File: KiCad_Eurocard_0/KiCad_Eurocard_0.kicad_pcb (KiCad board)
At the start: 2 copper layers, 1 part, among them IC1 ERA-1SM+

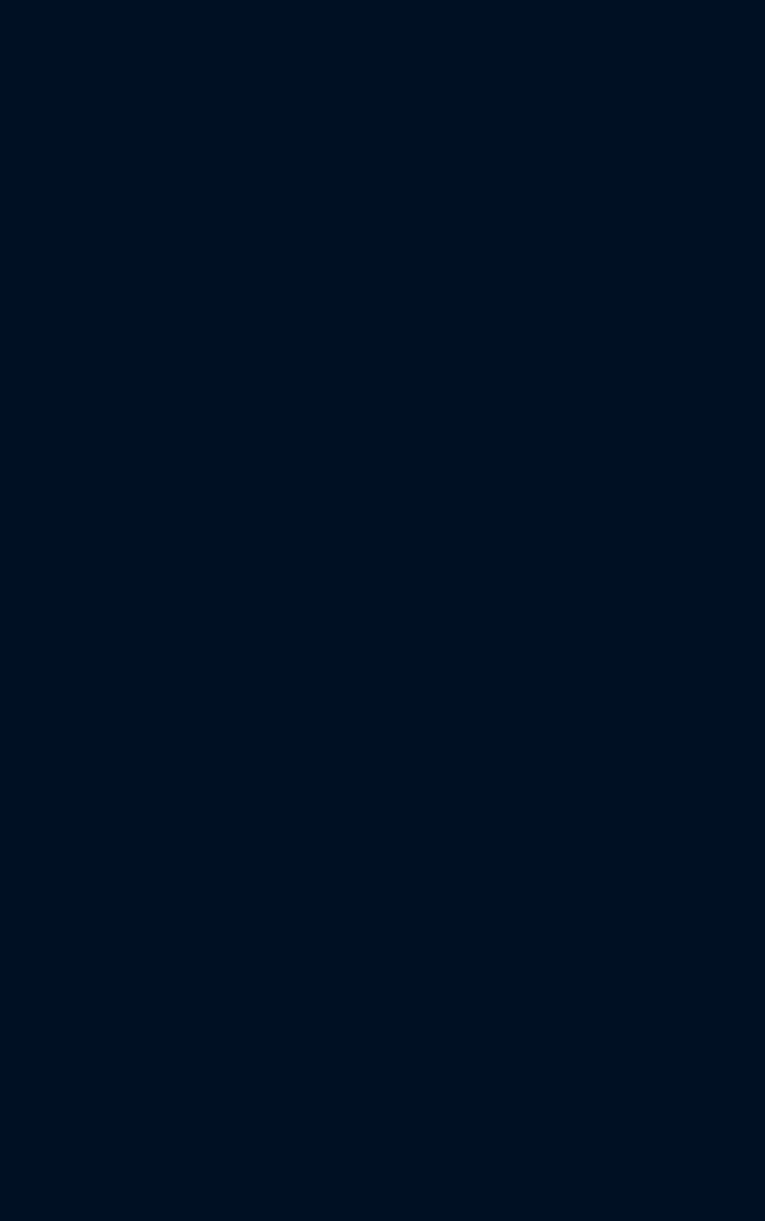
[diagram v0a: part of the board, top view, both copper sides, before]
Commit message: New Additions - Added new footprints
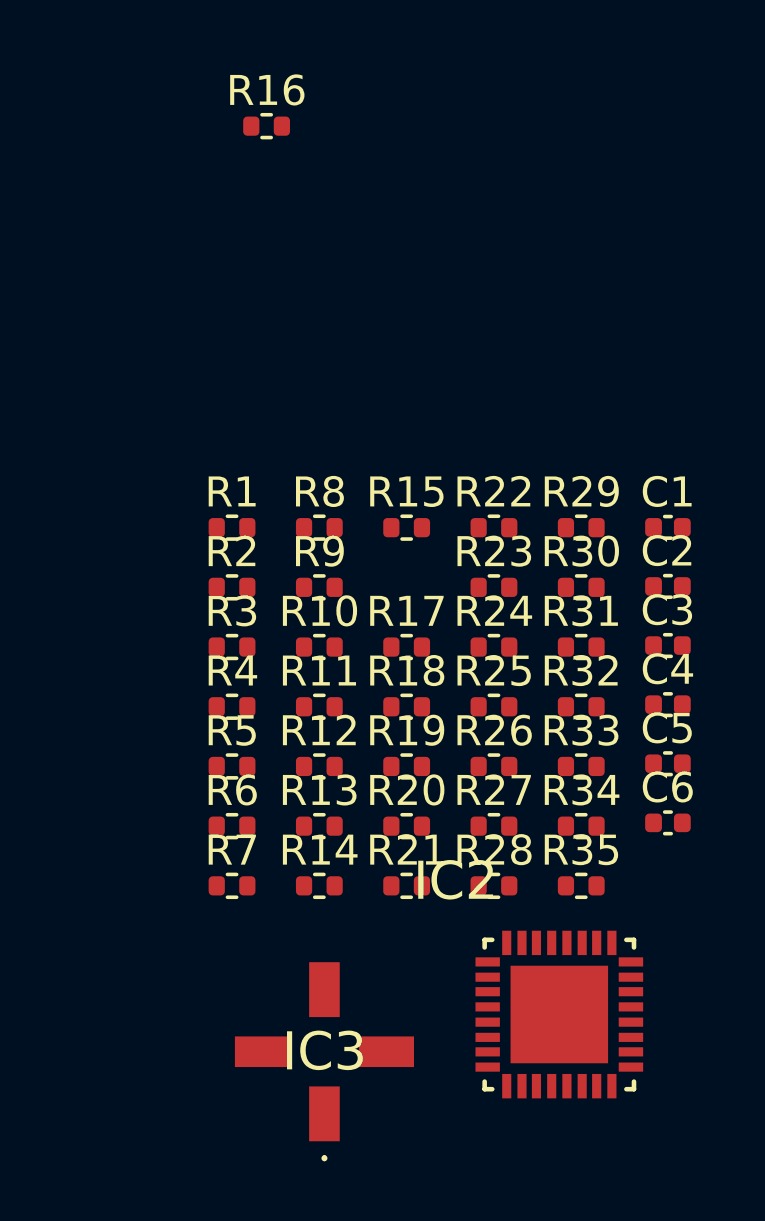
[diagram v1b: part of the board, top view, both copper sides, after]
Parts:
- added C1: C, Capacitor_SMD:C_0402_1005Metric, F.Cu at (108.9, 58.4)
- added C2: C, Capacitor_SMD:C_0402_1005Metric, F.Cu at (108.9, 60.3)
- added C3: C, Capacitor_SMD:C_0402_1005Metric, F.Cu at (108.9, 62.3)
- added C4: C, Capacitor_SMD:C_0402_1005Metric, F.Cu at (108.9, 64.3)
- added C5: C, Capacitor_SMD:C_0402_1005Metric, F.Cu at (108.9, 66.3)
- added C6: C, Capacitor_SMD:C_0402_1005Metric, F.Cu at (108.9, 68.2)
- added IC2: ADF4351BCPZ, ADF4351BPCZ:QFN50P500X500X100-33N, F.Cu at (105.2, 74.6)
- added IC3: ERA-1SM+, ERA-1SM+:ERA1SM, F.Cu at (97.4, 75.9)
- added R1: R, Resistor_SMD:R_0402_1005Metric, F.Cu at (94.3, 58.4)
- added R10: R, Resistor_SMD:R_0402_1005Metric, F.Cu at (97.2, 62.4)
- added R11: R, Resistor_SMD:R_0402_1005Metric, F.Cu at (97.2, 64.4)
- added R12: R, Resistor_SMD:R_0402_1005Metric, F.Cu at (97.2, 66.3)
- added R13: R, Resistor_SMD:R_0402_1005Metric, F.Cu at (97.2, 68.3)
- added R14: R, Resistor_SMD:R_0402_1005Metric, F.Cu at (97.2, 70.3)
- added R15: R, Resistor_SMD:R_0402_1005Metric, F.Cu at (100.2, 58.4)
- added R16: R, Resistor_SMD:R_0402_1005Metric, F.Cu at (95.5, 45.0)
- added R17: R, Resistor_SMD:R_0402_1005Metric, F.Cu at (100.2, 62.4)
- added R18: R, Resistor_SMD:R_0402_1005Metric, F.Cu at (100.2, 64.4)
- added R19: R, Resistor_SMD:R_0402_1005Metric, F.Cu at (100.2, 66.3)
- added R2: R, Resistor_SMD:R_0402_1005Metric, F.Cu at (94.3, 60.4)
- added R20: R, Resistor_SMD:R_0402_1005Metric, F.Cu at (100.2, 68.3)
- added R21: R, Resistor_SMD:R_0402_1005Metric, F.Cu at (100.2, 70.3)
- added R22: R, Resistor_SMD:R_0402_1005Metric, F.Cu at (103.1, 58.4)
- added R23: R, Resistor_SMD:R_0402_1005Metric, F.Cu at (103.1, 60.4)
- added R24: R, Resistor_SMD:R_0402_1005Metric, F.Cu at (103.1, 62.4)
- added R25: R, Resistor_SMD:R_0402_1005Metric, F.Cu at (103.1, 64.4)
- added R26: R, Resistor_SMD:R_0402_1005Metric, F.Cu at (103.1, 66.3)
- added R27: R, Resistor_SMD:R_0402_1005Metric, F.Cu at (103.1, 68.3)
- added R28: R, Resistor_SMD:R_0402_1005Metric, F.Cu at (103.1, 70.3)
- added R29: R, Resistor_SMD:R_0402_1005Metric, F.Cu at (106.0, 58.4)
- added R3: R, Resistor_SMD:R_0402_1005Metric, F.Cu at (94.3, 62.4)
- added R30: R, Resistor_SMD:R_0402_1005Metric, F.Cu at (106.0, 60.4)
- added R31: R, Resistor_SMD:R_0402_1005Metric, F.Cu at (106.0, 62.4)
- added R32: R, Resistor_SMD:R_0402_1005Metric, F.Cu at (106.0, 64.4)
- added R33: R, Resistor_SMD:R_0402_1005Metric, F.Cu at (106.0, 66.3)
- added R34: R, Resistor_SMD:R_0402_1005Metric, F.Cu at (106.0, 68.3)
- added R35: R, Resistor_SMD:R_0402_1005Metric, F.Cu at (106.0, 70.3)
- added R4: R, Resistor_SMD:R_0402_1005Metric, F.Cu at (94.3, 64.4)
- added R5: R, Resistor_SMD:R_0402_1005Metric, F.Cu at (94.3, 66.3)
- added R6: R, Resistor_SMD:R_0402_1005Metric, F.Cu at (94.3, 68.3)
- added R7: R, Resistor_SMD:R_0402_1005Metric, F.Cu at (94.3, 70.3)
- added R8: R, Resistor_SMD:R_0402_1005Metric, F.Cu at (97.2, 58.4)
- added R9: R, Resistor_SMD:R_0402_1005Metric, F.Cu at (97.2, 60.4)
- IC1: footprint KiCad:ERA1SM -> ERA-1SM+:ERA1SM
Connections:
- IC1 pad 1: unconnected-(IC1-RF_IN-Pad1) -> Net-(IC1-RF_IN)
- IC1 pad 2: unconnected-(IC1-GND_1-Pad2) -> GND
- IC1 pad 3: unconnected-(IC1-RF_-_OUT_AND_DC_-_IN-Pad3) -> Net-(IC1-RF_-_OUT_AND_DC_-_IN)
- IC1 pad 4: unconnected-(IC1-GND_2-Pad4) -> GND

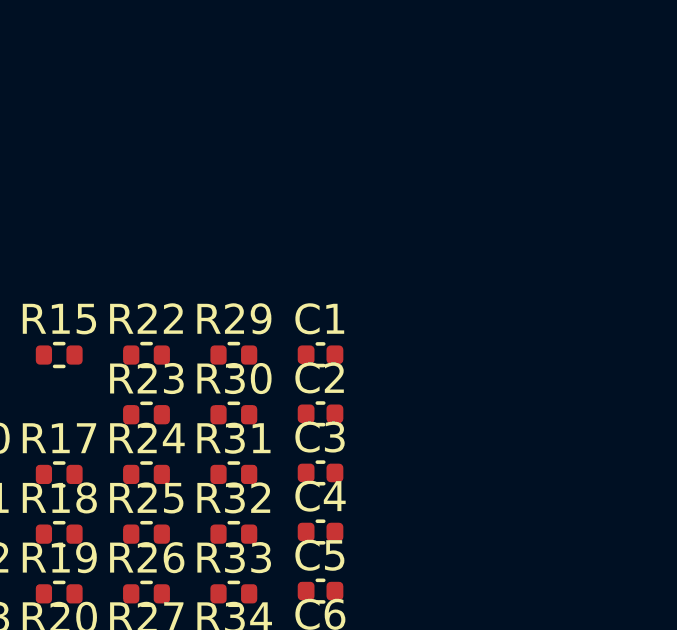
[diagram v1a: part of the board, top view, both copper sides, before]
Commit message: Changed wires to gobal nets
still need to figure out DDS and ADF4351
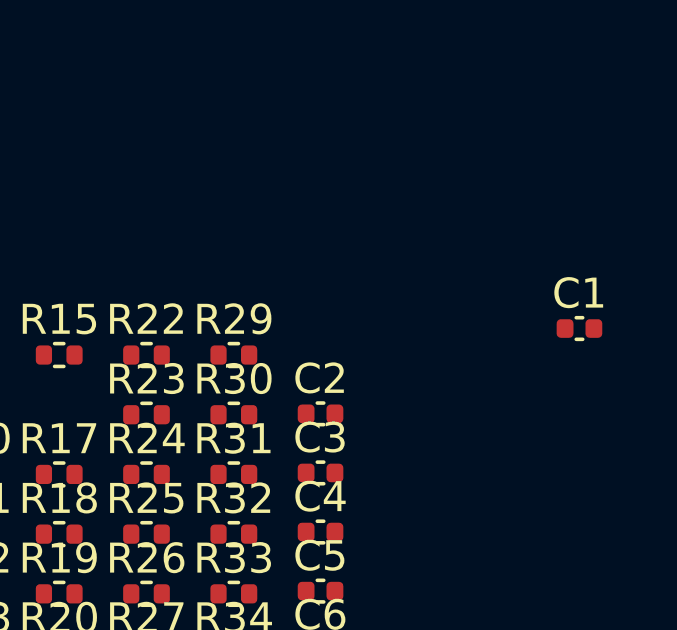
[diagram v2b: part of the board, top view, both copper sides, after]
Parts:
- moved C1 8.68 mm to (117.5, 57.5)
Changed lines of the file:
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@@
 	(footprint "Capacitor_SMD:C_0402_1005Metric"
 		(layer "F.Cu")
-		(at 108.8684 58.3734)
+		(at 117.5 57.5)
 		(descr "Capacitor SMD 0402 (1005 Metric), square (rectangular) end terminal, IPC-7351 nominal, (Body size source: IPC-SM-782 page 76, https://www.pcb-3d.com/wordpress/wp-content/uploads/ipc-sm-782a_amendment_1_and_2.pdf), generated with kicad-footprint-generator")
 		(tags "capacitor")

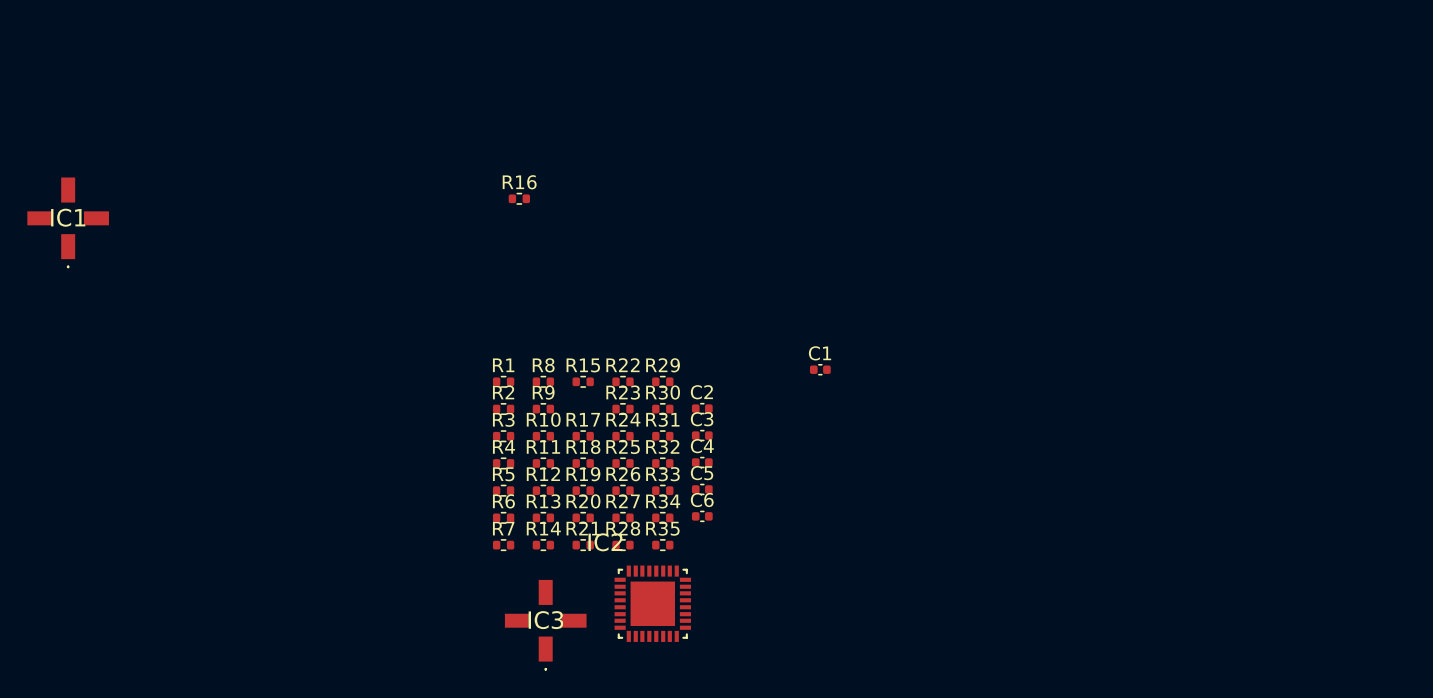
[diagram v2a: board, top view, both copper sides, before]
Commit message: ADF4351 Microcontroller Connecs. Done
- Added Microcontroller and connections to the ADF4351
- Started parameters note sheet
- Need to double check power is sufficient for circuit (hopefully, we can just use the 5V USB to power everything?)
- Need to make schematic look pretty as well/be more organized/labeled
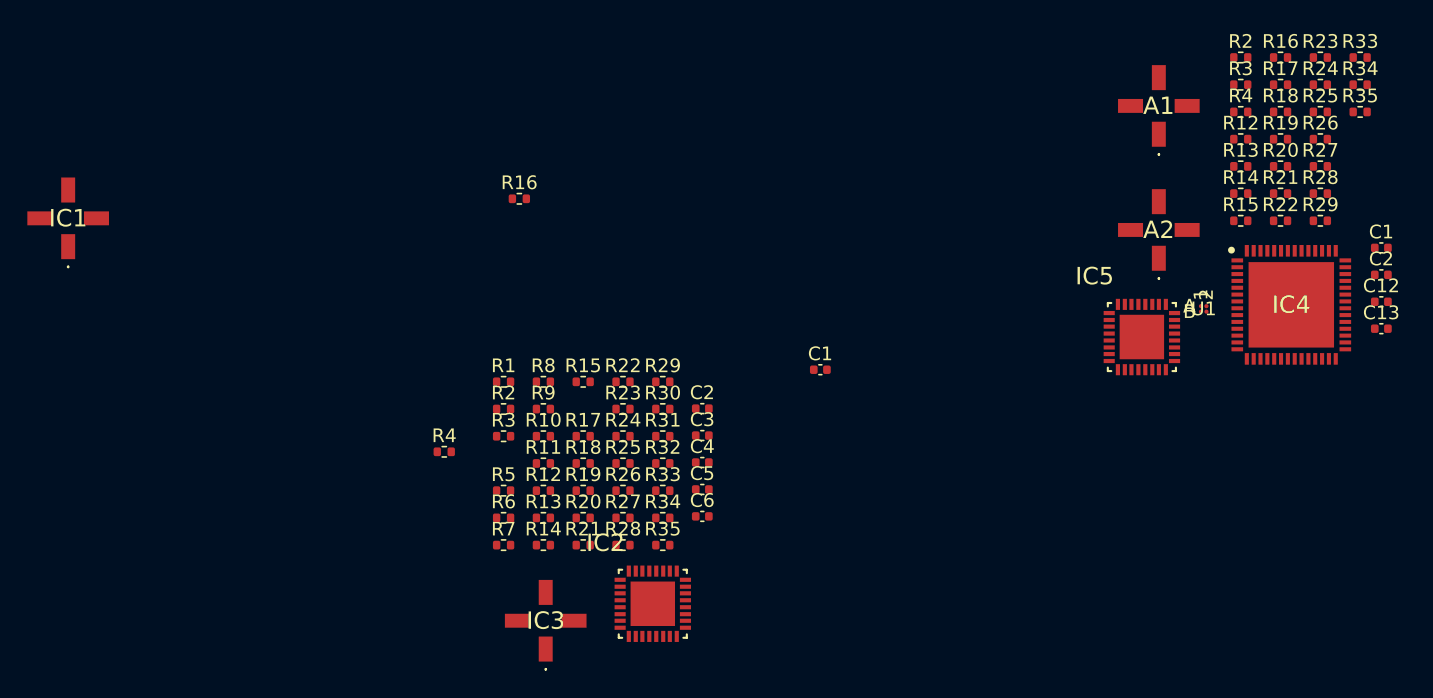
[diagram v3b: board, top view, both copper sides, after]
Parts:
- added A1: ERA-1SM+, ERA-1SM+:ERA1SM, F.Cu at (142.2, 38.2)
- added A2: ERA-1SM+, ERA-1SM+:ERA1SM, F.Cu at (142.2, 47.3)
- added C1: 300pF, Capacitor_SMD:C_0402_1005Metric, F.Cu at (158.5, 48.6)
- added C12: 300pF, Capacitor_SMD:C_0402_1005Metric, F.Cu at (158.5, 52.5)
- added C13: 300pF, Capacitor_SMD:C_0402_1005Metric, F.Cu at (158.5, 54.5)
- added C2: 300pF, Capacitor_SMD:C_0402_1005Metric, F.Cu at (158.5, 50.6)
- added IC4: AD9959BCPZ, KiCad:QFN50P800X800X100-57N-D, F.Cu at (151.9, 52.8)
- added IC5: ADF4351BCPZ, ADF4351BPCZ:QFN50P500X500X100-33N, F.Cu at (141.0, 55.1)
- added R12: 292.4 Ohms, Resistor_SMD:R_0402_1005Metric, F.Cu at (148.2, 40.6)
- added R13: 292.4 Ohms, Resistor_SMD:R_0402_1005Metric, F.Cu at (148.2, 42.6)
- added R14: 17.6 Ohms, Resistor_SMD:R_0402_1005Metric, F.Cu at (148.2, 44.6)
- added R15: 292.4 Ohms, Resistor_SMD:R_0402_1005Metric, F.Cu at (148.2, 46.6)
- added R16: 292.4 Ohms, Resistor_SMD:R_0402_1005Metric, F.Cu at (151.2, 34.7)
- added R17: 17.6 Ohms, Resistor_SMD:R_0402_1005Metric, F.Cu at (151.2, 36.7)
- added R18: 292.4 Ohms, Resistor_SMD:R_0402_1005Metric, F.Cu at (151.2, 38.6)
- added R19: 292.4 Ohms, Resistor_SMD:R_0402_1005Metric, F.Cu at (151.2, 40.6)
- added R2: 116.1 Ohms, Resistor_SMD:R_0402_1005Metric, F.Cu at (148.2, 34.7)
- added R20: 17.6 Ohms, Resistor_SMD:R_0402_1005Metric, F.Cu at (151.2, 42.6)
- added R21: 292.4 Ohms, Resistor_SMD:R_0402_1005Metric, F.Cu at (151.2, 44.6)
- added R22: 292.4 Ohms, Resistor_SMD:R_0402_1005Metric, F.Cu at (151.2, 46.6)
- added R23: 17.6 Ohms, Resistor_SMD:R_0402_1005Metric, F.Cu at (154.1, 34.7)
- added R24: 292.4 Ohms, Resistor_SMD:R_0402_1005Metric, F.Cu at (154.1, 36.7)
- added R25: 292.4 Ohms, Resistor_SMD:R_0402_1005Metric, F.Cu at (154.1, 38.6)
- added R26: 17.6 Ohms, Resistor_SMD:R_0402_1005Metric, F.Cu at (154.1, 40.6)
- added R27: 292.4 Ohms, Resistor_SMD:R_0402_1005Metric, F.Cu at (154.1, 42.6)
- added R28: 292.4 Ohms, Resistor_SMD:R_0402_1005Metric, F.Cu at (154.1, 44.6)
- added R29: 17.6 Ohms, Resistor_SMD:R_0402_1005Metric, F.Cu at (154.1, 46.6)
- added R3: 52.8 Ohms, Resistor_SMD:R_0402_1005Metric, F.Cu at (148.2, 36.7)
- added R33: 292.4 Ohms, Resistor_SMD:R_0402_1005Metric, F.Cu at (157.0, 34.7)
- added R34: 292.4 Ohms, Resistor_SMD:R_0402_1005Metric, F.Cu at (157.0, 36.7)
- added R35: 17.6 Ohms, Resistor_SMD:R_0402_1005Metric, F.Cu at (157.0, 38.6)
- added R4: 116.1 Ohms, Resistor_SMD:R_0402_1005Metric, F.Cu at (148.2, 38.6)
- added U1: ADP150ACBZ-2.85R7, ADP150:CB_4_3_ADI, F.Cu at (145.5, 53.1)
- R10, R32: value R -> 17.6 Ohms
- R11, R30, R31, R9: value R -> 292.4 Ohms
- R6, R8: value R -> 178.5 Ohms
- R7: value R -> 30.4 Ohms
- moved R4 4.42 mm to (90.0, 63.5)
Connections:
- net Net-(S1-PORT_3) renamed S1 Port 1
- net Net-(S2-PORT_5) renamed S2 Port 5
- net Net-(S2-SUM_PORT) renamed A2 OUT
- R6 pad 1: Net-(C5-Pad1) -> Net-(C2-Pad1)
- R7 pad 2: Net-(C5-Pad1) -> Net-(C2-Pad1)
